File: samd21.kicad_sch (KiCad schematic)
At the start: 40 parts, among them Q1 DTC043ZEB, Q2 DTC043ZEB, Q3 DTC043ZEB, SW1 SW_Push, SW2 SW_Push, U1 ATSAMD21J18A-M, U2 TXS0108EPW, Y1 MS1V-T1K_32768

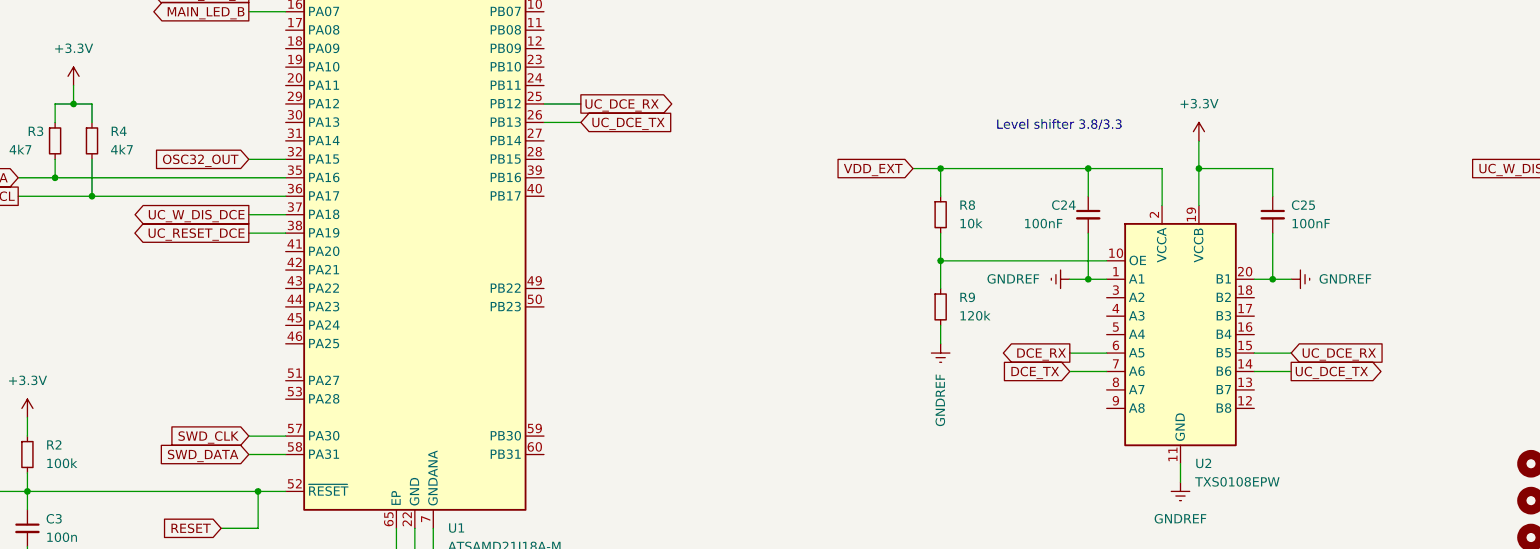
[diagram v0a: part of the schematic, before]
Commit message: added UART flow control pins CTS and RTS
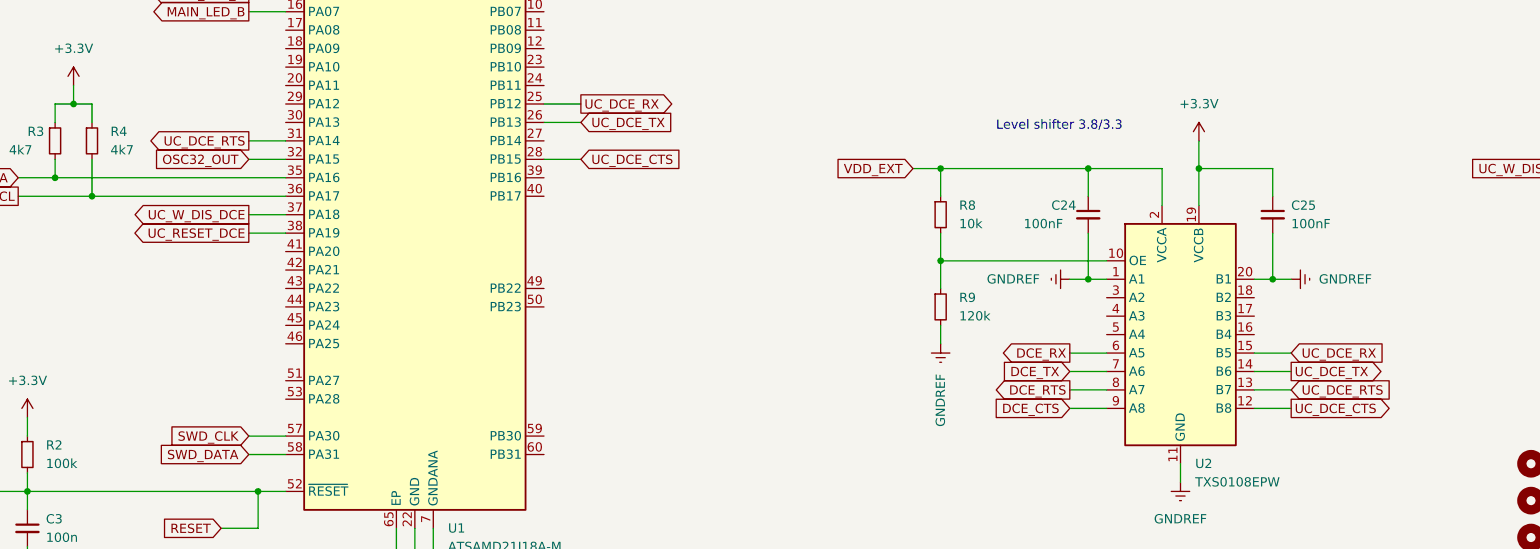
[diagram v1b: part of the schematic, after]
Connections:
- net UC_DCE_CTS: now reaches U1.28 (PB15)
- net UC_DCE_CTS: now also U2.12 (B8)
- net UC_DCE_RTS: now reaches U1.31 (PA14)
- net UC_DCE_RTS: now also U2.13 (B7)
- net DCE_RTS: now reaches U2.8 (A7)
- net DCE_CTS: now reaches U2.9 (A8)
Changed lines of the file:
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@@
+    (stroke (width 0) (type default) (color 0 0 0 0))
+  )
+  (wire (pts (xy 210.82 135.89) (xy 215.9 135.89))
     (stroke (width 0) (type default) (color 0 0 0 0))
   )
@@
     (stroke (width 0) (type default) (color 0 0 0 0))
   )
+  (wire (pts (xy 72.39 101.6) (xy 77.47 101.6))
+    (stroke (width 0) (type default) (color 0 0 0 0))
+  )
   (wire (pts (xy 39.37 68.58) (xy 39.37 69.85))
     (stroke (width 0) (type default) (color 0 0 0 0))
@@
     (stroke (width 0) (type default) (color 0 0 0 0))
   )
+  (wire (pts (xy 210.82 138.43) (xy 215.9 138.43))
+    (stroke (width 0) (type default) (color 0 0 0 0))
+  )
   (wire (pts (xy 162.56 54.61) (xy 162.56 55.88))
     (stroke (width 0) (type default) (color 0 0 0 0))
@@
     (stroke (width 0) (type default) (color 0 0 0 0))
   )
+  (wire (pts (xy 185.42 138.43) (xy 190.5 138.43))
+    (stroke (width 0) (type default) (color 0 0 0 0))
+  )
+  (wire (pts (xy 113.03 104.14) (xy 118.11 104.14))
+    (stroke (width 0) (type default) (color 0 0 0 0))
+  )
   (wire (pts (xy 17.78 149.86) (xy 20.32 149.86))
     (stroke (width 0) (type default) (color 0 0 0 0))
@@
   )
   (wire (pts (xy 50.8 96.52) (xy 50.8 99.06))
+    (stroke (width 0) (type default) (color 0 0 0 0))
+  )
+  (wire (pts (xy 185.42 135.89) (xy 190.5 135.89))
     (stroke (width 0) (type default) (color 0 0 0 0))
   )
@@
     (effects (font (size 1.27 1.27)) (justify left bottom))
   )
+  (global_label "DCE_CTS" (shape input) (at 185.42 138.43 180) (fields_autoplaced)
+    (effects (font (size 1.27 1.27)) (justify right))
+    (property "Intersheet References" "${INTERSHEET_REFS}" (id 0) (at 174.9031 138.3506 0)
+      (effects (font (size 1.27 1.27)) (justify right) hide)
+    )
+  )
   (global_label "MAIN_LED_G" (shape input) (at 34.29 189.23 180) (fields_autoplaced)
     (effects (font (size 1.27 1.27)) (justify right))
@@
     )
   )
+  (global_label "UC_DCE_CTS" (shape output) (at 215.9 138.43 0) (fields_autoplaced)
+    (effects (font (size 1.27 1.27)) (justify left))
+    (property "Intersheet References" "${INTERSHEET_REFS}" (id 0) (at 229.985 138.3506 0)
+      (effects (font (size 1.27 1.27)) (justify left) hide)
+    )
+  )
   (global_label "DCE_W_DISABLE" (shape output) (at 290.83 97.79 0) (fields_autoplaced)
     (effects (font (size 1.27 1.27)) (justify left))
@@
     )
   )
+  (global_label "UC_DCE_CTS" (shape input) (at 118.11 104.14 0) (fields_autoplaced)
+    (effects (font (size 1.27 1.27)) (justify left))
+    (property "Intersheet References" "${INTERSHEET_REFS}" (id 0) (at 132.195 104.2194 0)
+      (effects (font (size 1.27 1.27)) (justify left) hide)
+    )
+  )
+  (global_label "DCE_RTS" (shape output) (at 185.42 135.89 180) (fields_autoplaced)
+    (effects (font (size 1.27 1.27)) (justify right))
+    (property "Intersheet References" "${INTERSHEET_REFS}" (id 0) (at 174.9031 135.8106 0)
+      (effects (font (size 1.27 1.27)) (justify right) hide)
+    )
+  )
   (global_label "VDD_EXT" (shape input) (at 163.83 105.41 180) (fields_autoplaced)
     (effects (font (size 1.27 1.27)) (justify right))
@@
     )
   )
+  (global_label "UC_DCE_RTS" (shape output) (at 72.39 101.6 180) (fields_autoplaced)
+    (effects (font (size 1.27 1.27)) (justify right))
+    (property "Intersheet References" "${INTERSHEET_REFS}" (id 0) (at 58.305 101.5206 0)
+      (effects (font (size 1.27 1.27)) (justify right) hide)
+    )
+  )
+  (global_label "UC_DCE_RTS" (shape input) (at 215.9 135.89 0) (fields_autoplaced)
+    (effects (font (size 1.27 1.27)) (justify left))
+    (property "Intersheet References" "${INTERSHEET_REFS}" (id 0) (at 229.985 135.8106 0)
+      (effects (font (size 1.27 1.27)) (justify left) hide)
+    )
+  )

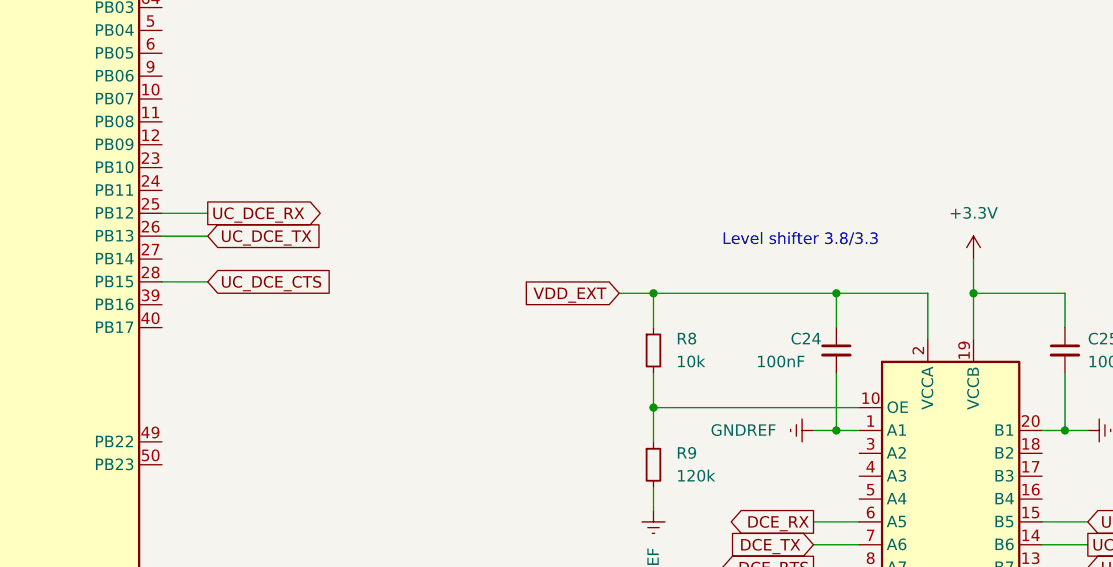
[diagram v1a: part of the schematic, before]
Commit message: 3.8V LDO: added output enable control from uc
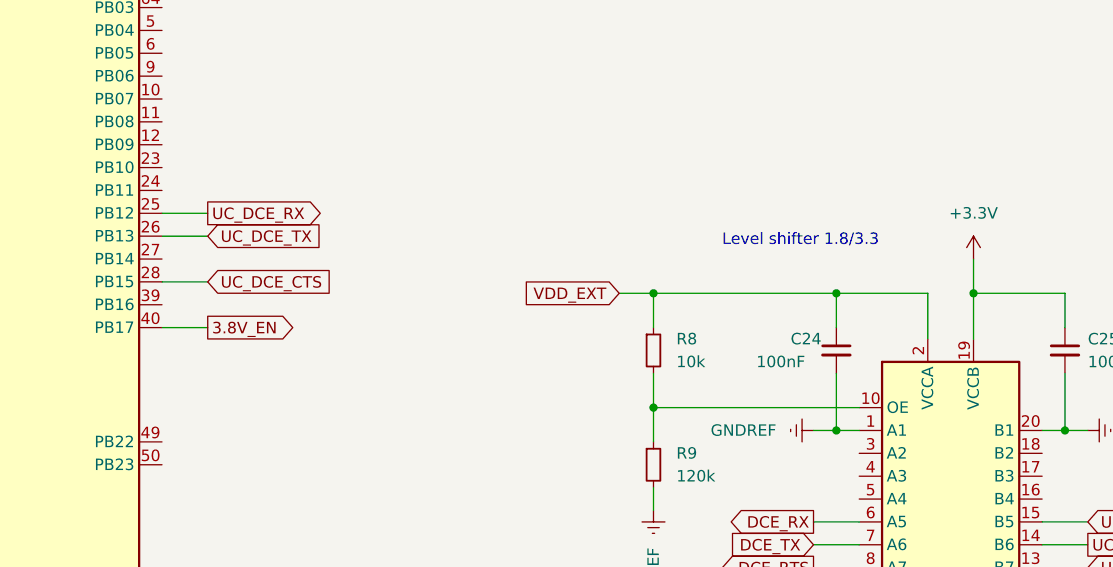
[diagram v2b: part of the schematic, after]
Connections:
- net 3.8V_EN: now reaches U1.40 (PB17)
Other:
- note added: "Level shifter 1.8/3.3"
- note removed: "Level shifter 3.8/3.3"
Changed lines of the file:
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@@
+    (stroke (width 0) (type default) (color 0 0 0 0))
+  )
+  (wire (pts (xy 113.03 109.22) (xy 118.11 109.22))
     (stroke (width 0) (type default) (color 0 0 0 0))
   )
@@
     (stroke (width 0) (type default) (color 0 0 0 0))
   )
-  (text "Level shifter 3.8/3.3" (at 175.26 100.33 0)
+  (text "Level shifter 1.8/3.3" (at 175.26 100.33 0)
     (effects (font (size 1.27 1.27)) (justify left bottom))
   )
@@
     )
   )
+  (global_label "3.8V_EN" (shape output) (at 118.11 109.22 0) (fields_autoplaced)
+    (effects (font (size 1.27 1.27)) (justify left))
+    (property "Intersheet References" "${INTERSHEET_REFS}" (id 0) (at 128.0826 109.1406 0)
+      (effects (font (size 1.27 1.27)) (justify left) hide)
+    )
+  )

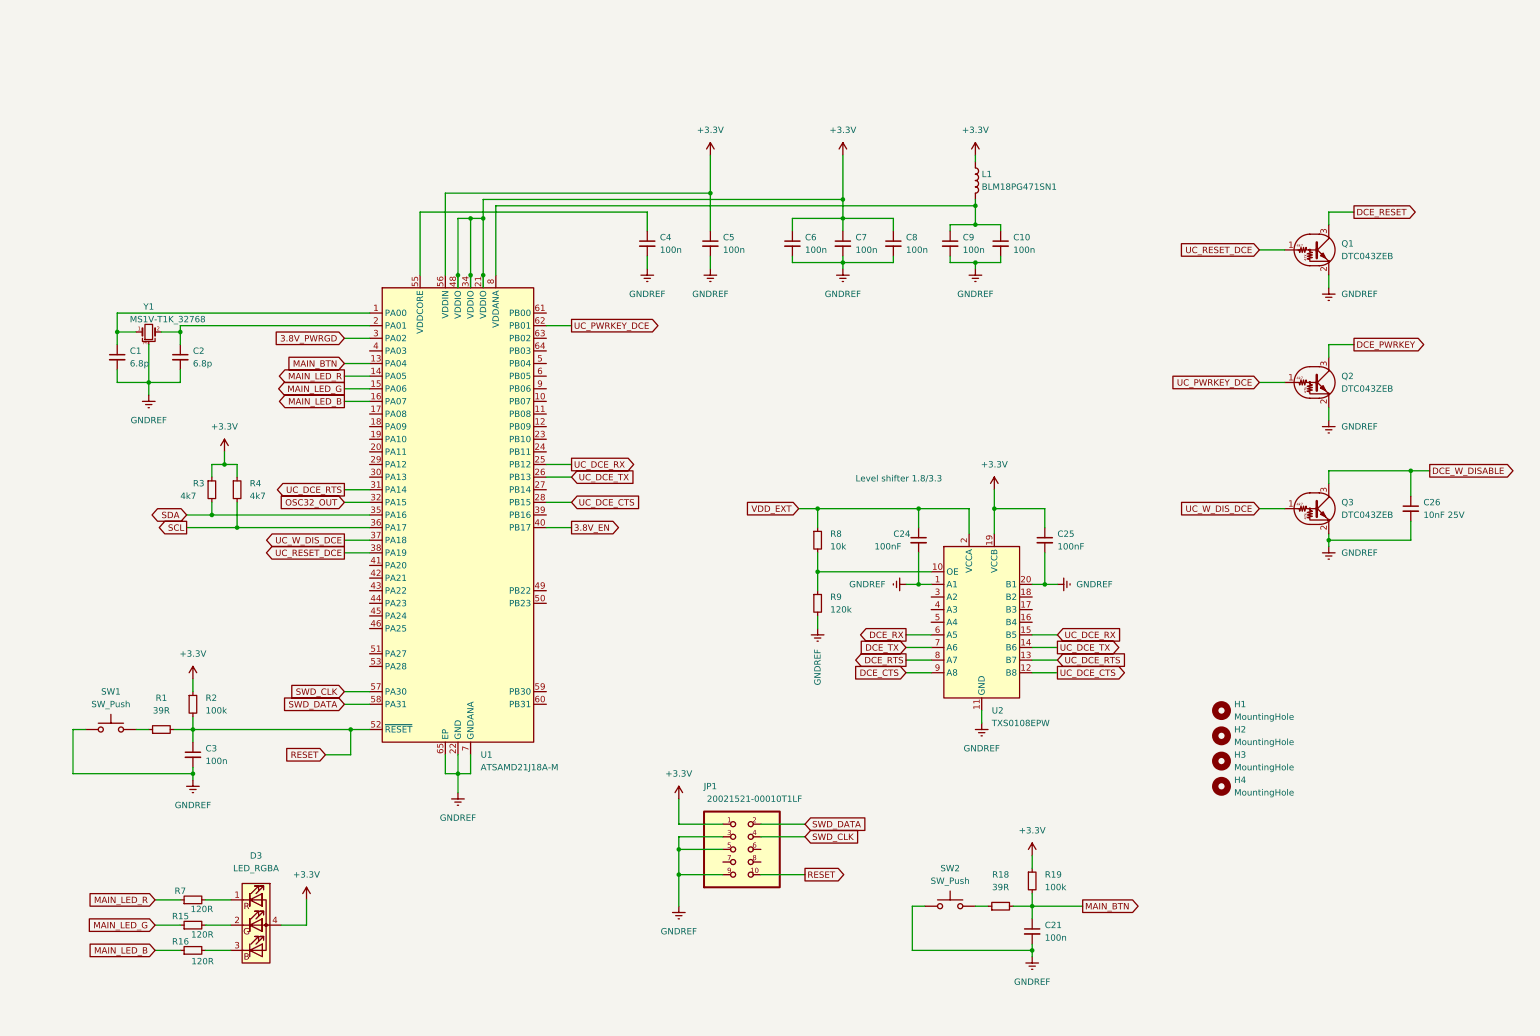
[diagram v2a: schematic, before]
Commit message: added connectors for I2C and SPI extensions
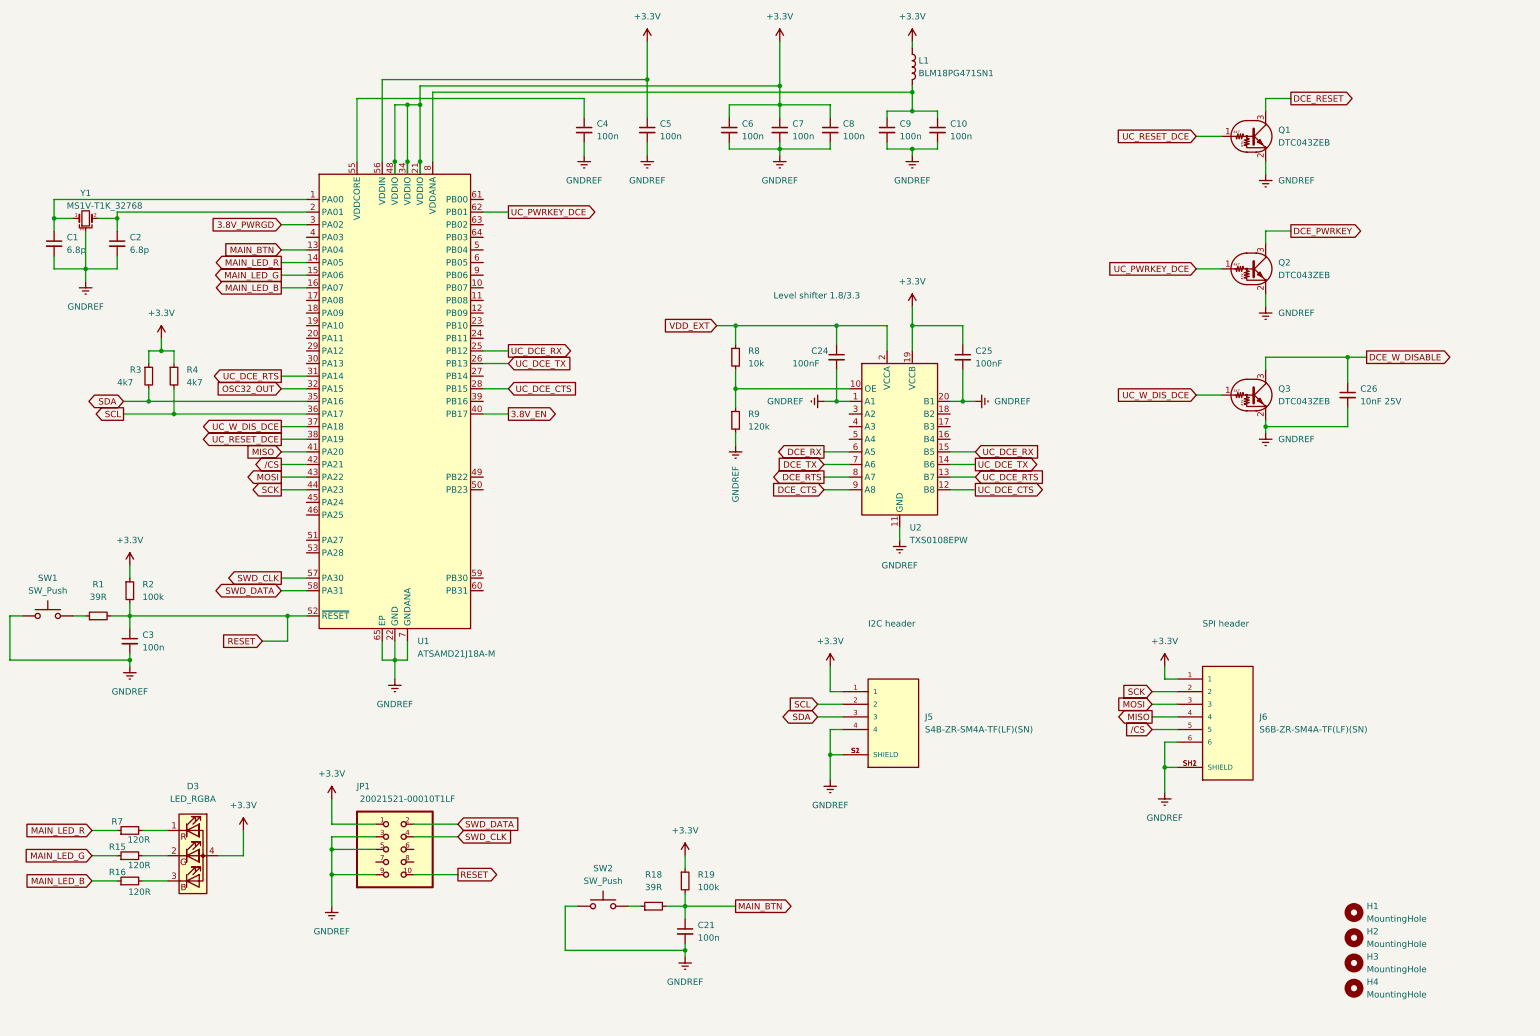
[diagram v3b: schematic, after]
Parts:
- added J5: S4B-ZR-SM4A-TF(LF)(SN), S4B-ZR-SM4A-TF_LF__SN_:JST_S4B-ZR-SM4A-TF(LF)(SN), symbol S4B-ZR-SM4A-TF_LF__SN_:S4B-ZR-SM4A-TF(LF)(SN)
- added J6: S6B-ZR-SM4A-TF(LF)(SN), S6B-ZR-SM4A-TF_LF__SN_:JST_S6B-ZR-SM4A-TF(LF)(SN), symbol S6B-ZR-SM4A-TF_LF__SN_:S6B-ZR-SM4A-TF(LF)(SN)
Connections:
- net +3V3: now also J5.1, J6.1
- net GNDREF: now also J5.4, J5.S1 (SHIELD), J5.S2 (SHIELD), J6.6, J6.SH1 (SHIELD), J6.SH2 (SHIELD)
- net SCL: now also J5.2
- net SDA: now also J5.3
- net MISO: now reaches U1.41 (PA20)
- net MISO: now also J6.4
- net /CS: now reaches U1.42 (PA21)
- net /CS: now also J6.5
- net MOSI: now reaches U1.43 (PA22)
- net MOSI: now also J6.3
- net SCK: now reaches U1.44 (PA23)
- net SCK: now also J6.2
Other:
- note added: "I2C header"
- note added: "SPI header"
- moved on the sheet: C1, C10, C2, C21, C24, C25, C26, C3, C4, C5, C6, C7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

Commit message: ok before switching to EG91EX footprint
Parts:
- SW1, SW2: footprint Button_Switch_SMD:SW_SPST_CK_KXT3 -> Button_Switch_SMD:SW_Push_1P1T_NO_CK_KMR2
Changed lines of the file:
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@@
     (property "Reference" "SW2" (id 0) (at 124.46 177.8 0))
     (property "Value" "SW_Push" (id 1) (at 124.46 180.34 0))
-    (property "Footprint" "Button_Switch_SMD:SW_SPST_CK_KXT3" (id 2) (at 124.46 180.34 0)
+    (property "Footprint" "Button_Switch_SMD:SW_Push_1P1T_NO_CK_KMR2" (id 2) (at 124.46 180.34 0)
       (effects (font (size 1.27 1.27)) hide)
     )
@@
     (property "Reference" "SW1" (id 0) (at 12.7 119.38 0))
     (property "Value" "SW_Push" (id 1) (at 12.7 121.92 0))
-    (property "Footprint" "Button_Switch_SMD:SW_SPST_CK_KXT3" (id 2) (at 12.7 121.92 0)
-      (effects (font (size 1.27 1.27)) hide)
-    )
+    (property "Footprint" "Button_Switch_SMD:SW_Push_1P1T_NO_CK_KMR2" (id 2) (at 12.7 121.92 0)
+      (effects (font (size 1.27 1.27)) hide)
+    )
